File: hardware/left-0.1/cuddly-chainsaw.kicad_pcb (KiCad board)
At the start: 2 copper layers, 162 x 100.8 mm, 132 parts, among them J1 USB_C_Receptacle_USB2.0, J2 USB_C_Receptacle_USB2.0, J3 AVR-ISP-6, SW1 Encoder_MX_RGB, SW10 MX_RGB, SW11 MX_RGB, SW12 MX_RGB, SW13 MX_RGB, SW14 MX_RGB, SW15 MX_RGB, SW16 MX_RGB, SW17 MX_RGB, SW18 MX_RGB, SW19 MX_RGB, SW2 MX_RGB, SW20 MX_RGB, SW21 MX_RGB, SW22 MX_RGB, SW23 MX_RGB, SW24 MX_RGB, SW25 MX_RGB, SW26 MX_RGB, SW27 MX_RGB, SW28 MX_RGB, SW29 MX_RGB, SW3 MX_RGB, SW30 MX_RGB, SW31 MX_RGB, SW32 MX_RGB, SW33 MX_RGB, SW34 MX_RGB, SW35 SW_Push, SW4 MX_RGB, SW5 MX_RGB, SW6 MX_RGB, SW7 MX_RGB, SW8 MX_RGB, SW9 MX_RGB, U1 USBLC6-2SC6, U2 ATmega32U4-MU, Y1 16MHz

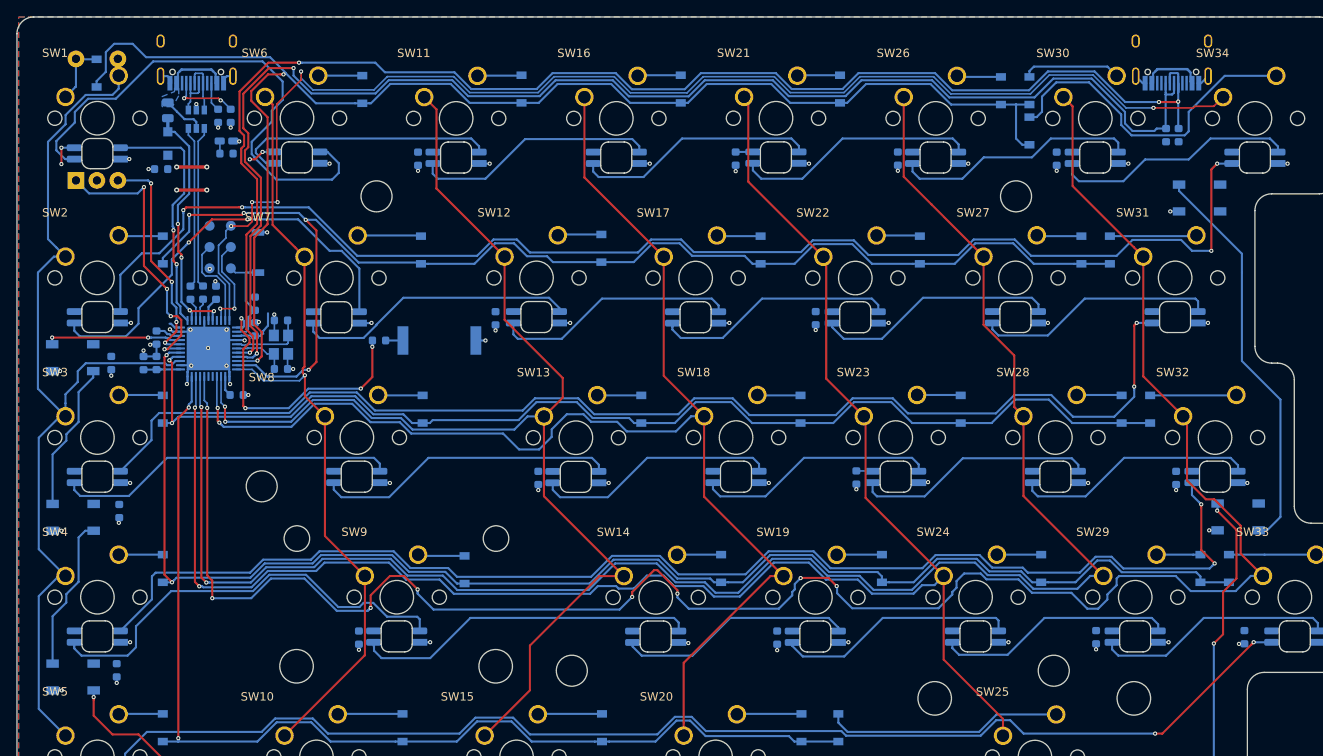
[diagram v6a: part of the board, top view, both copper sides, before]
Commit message: update board with new footprints
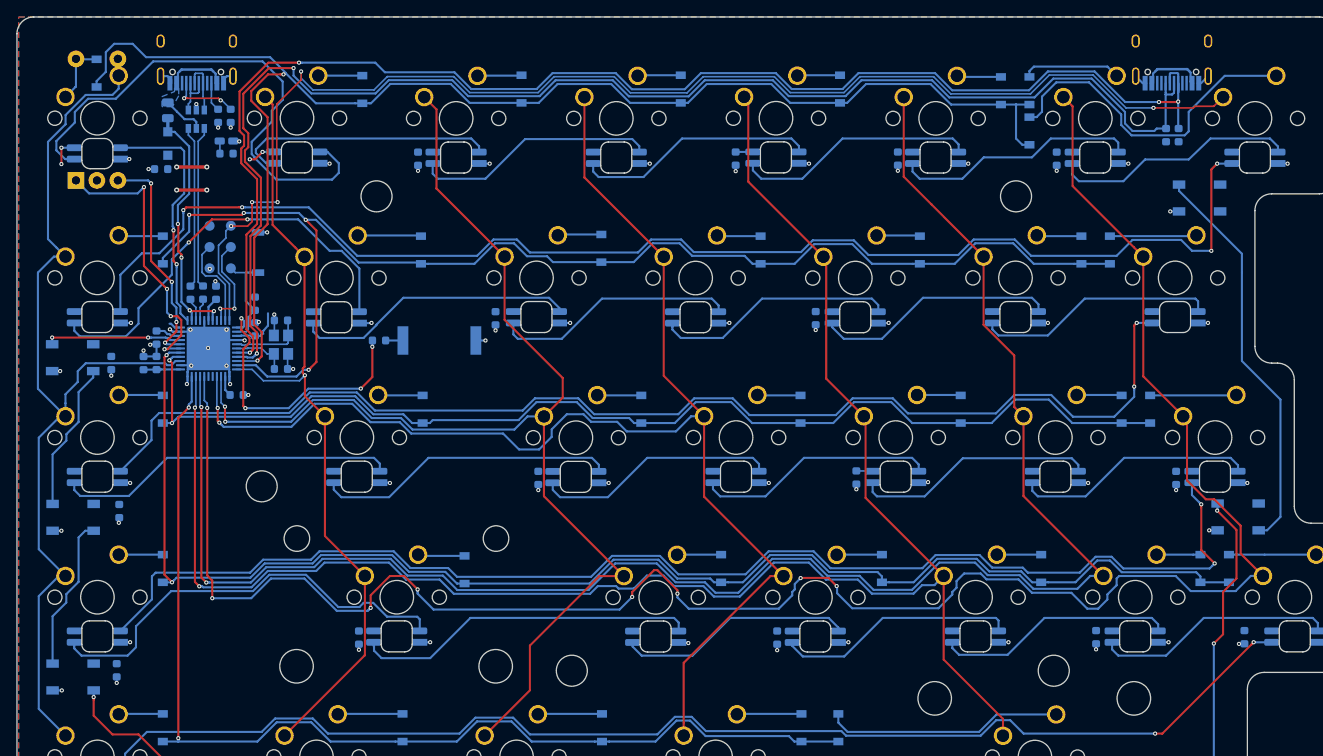
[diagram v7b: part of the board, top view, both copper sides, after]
